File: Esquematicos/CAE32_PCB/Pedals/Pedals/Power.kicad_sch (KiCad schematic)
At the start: 16 parts, among them U5 LDL1117

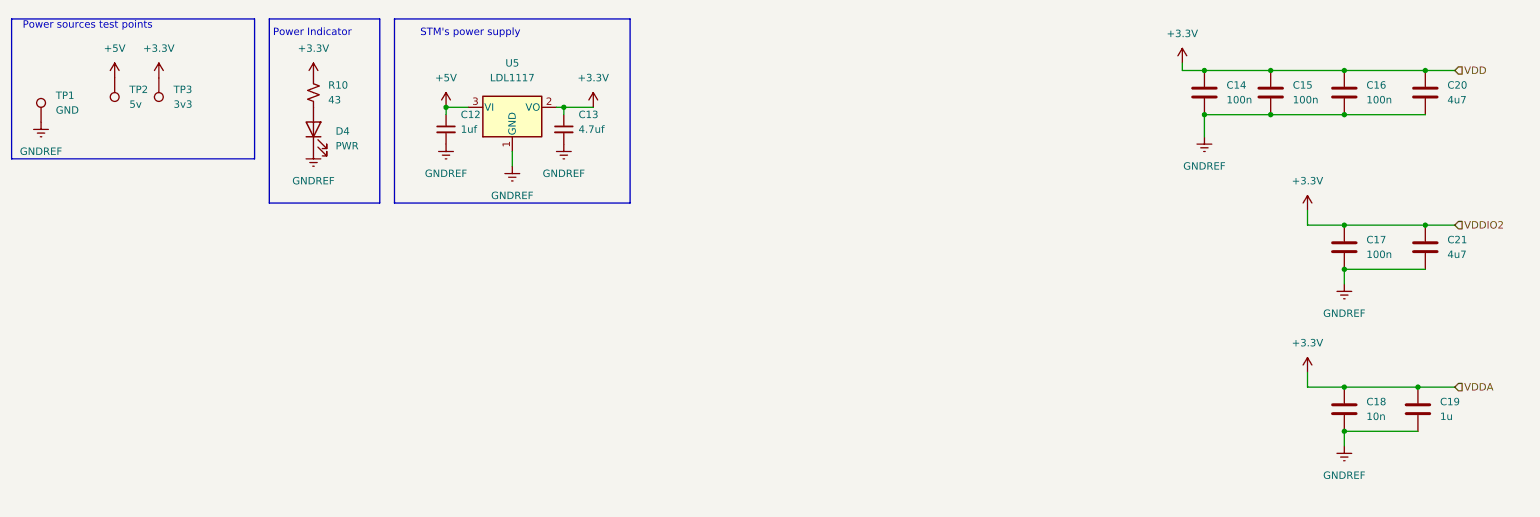
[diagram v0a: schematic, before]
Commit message: update: se añade otra hoja para las celdas de carga, ademas de reorganizar todas las hojas
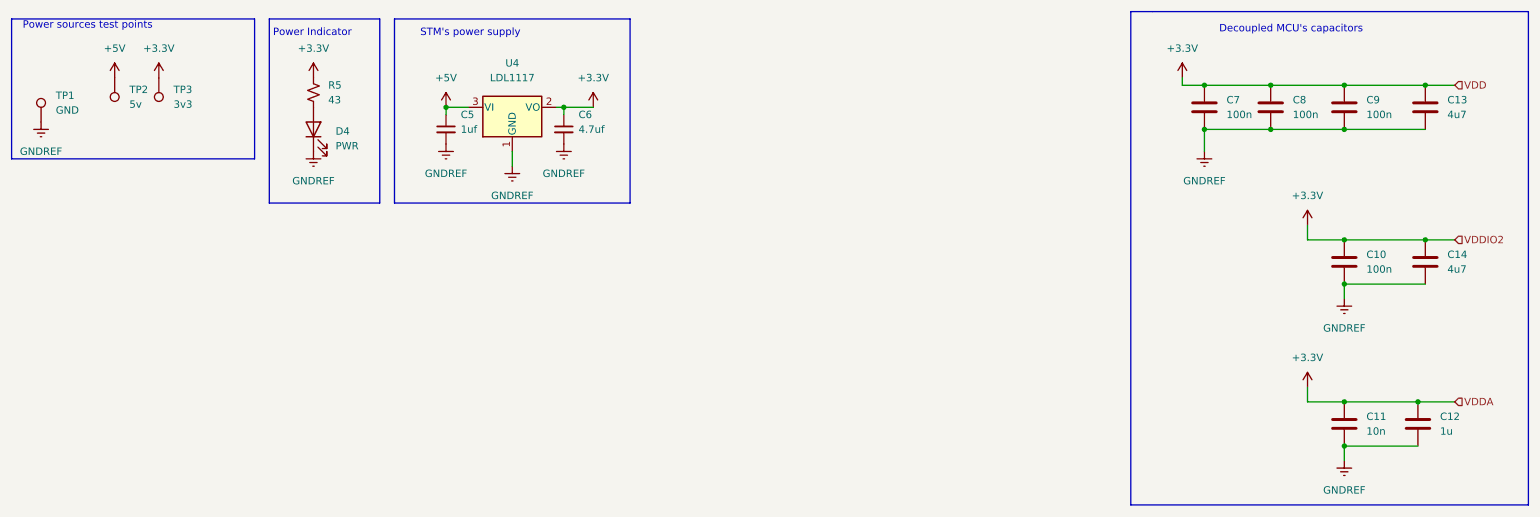
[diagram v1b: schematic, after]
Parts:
- C10: renamed from C17; footprint Capacitor_SMD:C_0805_2012Metric_Pad1.18x1.45mm_HandSolder -> Capacitor_SMD:C_0603_1608Metric_Pad1.08x0.95mm_HandSolder
- C11: renamed from C18; footprint Capacitor_SMD:C_0805_2012Metric_Pad1.18x1.45mm_HandSolder -> Capacitor_SMD:C_0603_1608Metric_Pad1.08x0.95mm_HandSolder
- C12: renamed from C19; footprint Capacitor_SMD:C_0805_2012Metric_Pad1.18x1.45mm_HandSolder -> Capacitor_SMD:C_0603_1608Metric_Pad1.08x0.95mm_HandSolder
- C13: renamed from C20; footprint Capacitor_SMD:C_0805_2012Metric_Pad1.18x1.45mm_HandSolder -> Capacitor_SMD:C_0603_1608Metric_Pad1.08x0.95mm_HandSolder
- C14: renamed from C21; footprint Capacitor_SMD:C_0805_2012Metric_Pad1.18x1.45mm_HandSolder -> Capacitor_SMD:C_0603_1608Metric_Pad1.08x0.95mm_HandSolder
- C5: renamed from C12; footprint Capacitor_SMD:C_0805_2012Metric_Pad1.18x1.45mm_HandSolder -> Capacitor_SMD:C_0603_1608Metric_Pad1.08x0.95mm_HandSolder
- C6: renamed from C13; footprint Capacitor_SMD:C_0805_2012Metric_Pad1.18x1.45mm_HandSolder -> Capacitor_SMD:C_0603_1608Metric_Pad1.08x0.95mm_HandSolder
- C7: renamed from C14; footprint Capacitor_SMD:C_0805_2012Metric_Pad1.18x1.45mm_HandSolder -> Capacitor_SMD:C_0603_1608Metric_Pad1.08x0.95mm_HandSolder
- C8: renamed from C15; footprint Capacitor_SMD:C_0805_2012Metric_Pad1.18x1.45mm_HandSolder -> Capacitor_SMD:C_0603_1608Metric_Pad1.08x0.95mm_HandSolder
- C9: renamed from C16; footprint Capacitor_SMD:C_0805_2012Metric_Pad1.18x1.45mm_HandSolder -> Capacitor_SMD:C_0603_1608Metric_Pad1.08x0.95mm_HandSolder
- renumbered R10 to R5, U5 to U4
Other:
- note added: "Decoupled MCU's capacitors"
- moved on the sheet: C10, C11, C12, C13, C14, C7, C8, C9

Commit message: update: Componentes acomodados en la PCB
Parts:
- R5: footprint Resistor_SMD:R_0805_2012Metric_Pad1.20x1.40mm_HandSolder -> Resistor_SMD:R_0603_1608Metric_Pad0.98x0.95mm_HandSolder
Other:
- moved on the sheet: C10, C11, C12, C13, C14, C7, C8, C9

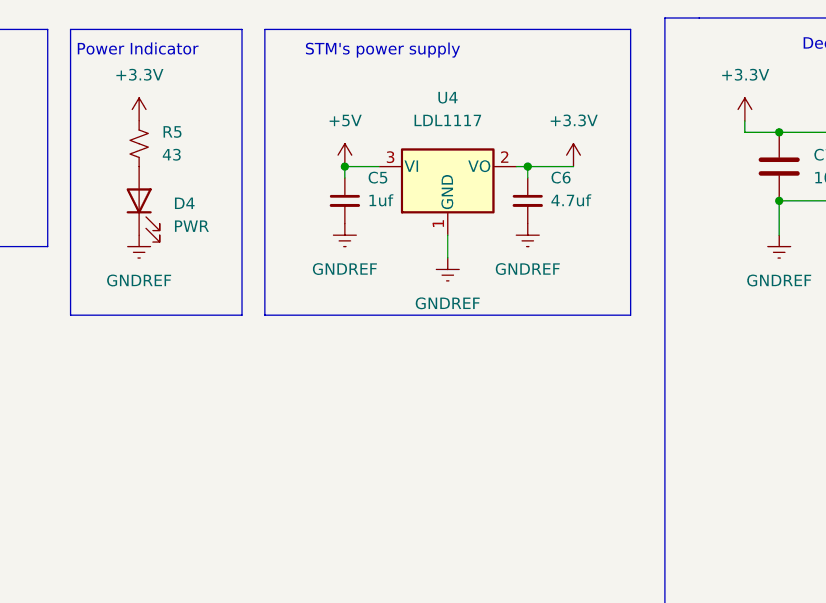
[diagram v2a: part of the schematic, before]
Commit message: update: se agrega el consumo de corriente a los IC's ademas de agregar el URL y numero de parte de los componentes de LCSC en kicad
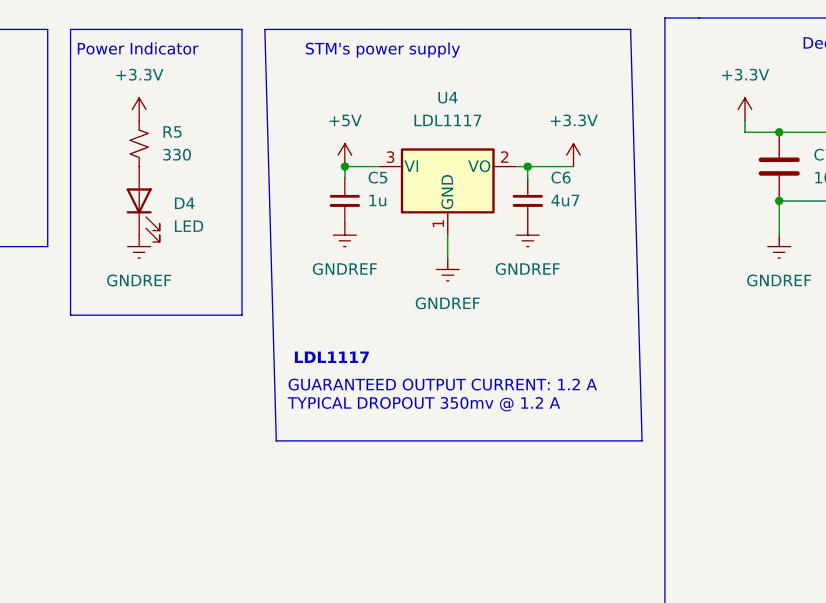
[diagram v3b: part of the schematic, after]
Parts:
- C10, C7, C8, C9: LCSC_PART (none) -> c1591
- C11: LCSC_PART (none) -> C100042
- C12: LCSC_PART (none) -> C1592
- C13, C14: LCSC_PART (none) -> C1705
- C5: value 1uf -> 1u; LCSC_PART (none) -> C1592
- C6: value 4.7uf -> 4u7; LCSC_PART (none) -> C1705
- D4: value PWR -> LED; LCSC_PART (none) -> C965815
- R5: value 43 -> 330; LCSC_PART (none) -> C25804
- U4: LCSC_PART (none) -> C2798214
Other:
- note added: "GUARANTEED OUTPUT CURRENT: 1.2 A TYPICAL DROPOUT 350mv @ 1.2 A"
- note added: "LDL1117"
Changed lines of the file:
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@@
     (stroke (width 0) (type default) (color 0 0 0 0))
   )
-  (polyline (pts (xy 125.73 21.59) (xy 125.73 53.34))
+  (polyline (pts (xy 125.73 21.59) (xy 127 67.31))
     (stroke (width 0) (type default) (color 0 0 0 0))
   )
@@
     (stroke (width 0) (type default) (color 0 0 0 0))
   )
-  (polyline (pts (xy 85.09 21.59) (xy 85.09 53.34))
+  (polyline (pts (xy 85.09 21.59) (xy 86.36 67.31))
     (stroke (width 0) (type default) (color 0 0 0 0))
   )
@@
     (stroke (width 0) (type default) (color 0 0 0 0))
   )
-  (polyline (pts (xy 125.73 53.34) (xy 85.09 53.34))
+  (polyline (pts (xy 127 67.31) (xy 86.36 67.31))
     (stroke (width 0) (type default) (color 0 0 0 0))
   )
@@
     (effects (font (size 1.27 1.27)) (justify left bottom))
   )
+  (text "GUARANTEED OUTPUT CURRENT: 1.2 A\nTYPICAL DROPOUT 350mv @ 1.2 A"
+    (at 87.63 64.135 0)
+    (effects (font (size 1.27 1.27)) (justify left bottom))
+  )
   (text "STM's power supply" (at 89.535 24.765 0)
     (effects (font (size 1.27 1.27)) (justify left bottom))
@@
   (text "Power sources test points" (at 20.955 23.495 0)
     (effects (font (size 1.27 1.27)) (justify left bottom))
+  )
+  (text "LDL1117" (at 88.265 59.055 0)
+    (effects (font (size 1.27 1.27) bold) (justify left bottom))
   )
   (hierarchical_label "VDDA" (shape input) (at 185.42 87.63 0)
@@
       (effects (font (size 1.27 1.27)) hide)
     )
+    (property "LCSC_PART" "C2798214" (id 4) (at 105.41 36.83 0)
+      (effects (font (size 1.27 1.27)) hide)
+    )
     (pin "1")
     (pin "2")
@@
     )
     (property "Datasheet" "~" (id 3) (at 166.37 36.83 0)
+      (effects (font (size 1.27 1.27)) hide)
+    )
+    (property "LCSC_PART" "c1591" (id 4) (at 166.37 36.83 0)
       (effects (font (size 1.27 1.27)) hide)
     )
@@
       (effects (font (size 1.27 1.27)) (justify left))
     )
-    (property "Value" "43" (id 1) (at 73.66 35.5599 0)
+    (property "Value" "330" (id 1) (at 73.66 35.5599 0)
       (effects (font (size 1.27 1.27)) (justify left))
     )
@@
       (effects (font (size 1.27 1.27)) hide)
     )
+    (property "LCSC_PART" "C25804" (id 4) (at 71.12 34.29 0)
+      (effects (font (size 1.27 1.27)) hide)
+    )
     (pin "1")
     (pin "2")
@@
       (effects (font (size 1.27 1.27)) hide)
     )
-    (property "Datasheet" "~" (id 3) (at 29.21 39.37 0)
+    (property "Datasheet" "" (id 3) (at 29.21 39.37 0)
+      (effects (font (size 1.27 1.27)) hide)
+    )
+    (property "LCSC_PART" "" (id 4) (at 24.13 39.37 0)
       (effects (font (size 1.27 1.27)) hide)
     )
@@
       (effects (font (size 1.27 1.27)) hide)
     )
+    (property "LCSC_PART" "C1705" (id 4) (at 180.34 63.5 0)
+      (effects (font (size 1.27 1.27)) hide)
+    )
     (pin "1")
     (pin "2")
@@
       (effects (font (size 1.27 1.27)) hide)
     )
+    (property "LCSC_PART" "c1591" (id 4) (at 166.37 63.5 0)
+      (effects (font (size 1.27 1.27)) hide)
+    )
     (pin "1")
     (pin "2")
@@
     )
     (property "Datasheet" "~" (id 3) (at 180.34 36.83 0)
+      (effects (font (size 1.27 1.27)) hide)
+    )
+    (property "LCSC_PART" "C1705" (id 4) (at 180.34 36.83 0)
       (effects (font (size 1.27 1.27)) hide)
     )
@@
       (effects (font (size 1.27 1.27)) (justify left))
     )
-    (property "Value" "4.7uf" (id 1) (at 116.84 40.64 0)
+    (property "Value" "4u7" (id 1) (at 116.84 40.64 0)
       (effects (font (size 1.27 1.27)) (justify left))
     )
@@
     )
     (property "Datasheet" "~" (id 3) (at 114.3 40.64 0)
+      (effects (font (size 1.27 1.27)) hide)
+    )
+    (property "LCSC_PART" "C1705" (id 4) (at 114.3 40.64 0)
       (effects (font (size 1.27 1.27)) hide)
     )
@@
       (effects (font (size 1.27 1.27)) hide)
     )
-    (property "Datasheet" "~" (id 3) (at 179.07 91.44 0)
+    (property "Datasheet" "" (id 3) (at 179.07 91.44 0)
+      (effects (font (size 1.27 1.27)) hide)
+    )
+    (property "LCSC_PART" "C1592" (id 4) (at 179.07 91.44 0)
       (effects (font (size 1.27 1.27)) hide)
     )
@@
     )
     (property "Datasheet" "~" (id 3) (at 142.24 36.83 0)
+      (effects (font (size 1.27 1.27)) hide)
+    )
+    (property "LCSC_PART" "c1591" (id 4) (at 142.24 36.83 0)
       (effects (font (size 1.27 1.27)) hide)
     )
@@
       (effects (font (size 1.27 1.27)) (justify left))
     )
-    (property "Value" "1uf" (id 1) (at 96.52 40.64 0)
+    (property "Value" "1u" (id 1) (at 96.52 40.64 0)
       (effects (font (size 1.27 1.27)) (justify left))
     )
@@
       (effects (font (size 1.27 1.27)) hide)
     )
-    (property "Datasheet" "~" (id 3) (at 93.98 40.64 0)
+    (property "Datasheet" "" (id 3) (at 93.98 40.64 0)
+      (effects (font (size 1.27 1.27)) hide)
+    )
+    (property "LCSC_PART" "C1592" (id 4) (at 93.98 40.64 0)
       (effects (font (size 1.27 1.27)) hide)
     )
@@
       (effects (font (size 1.27 1.27)) hide)
     )
+    (property "LCSC_PART" "C100042" (id 4) (at 166.37 91.44 0)
+      (effects (font (size 1.27 1.27)) hide)
+    )
     (pin "1")
     (pin "2")
@@
       (effects (font (size 1.27 1.27)) (justify right))
     )
-    (property "Value" "PWR" (id 1) (at 74.93 43.4974 90)
+    (property "Value" "LED" (id 1) (at 74.93 43.4974 90)
       (effects (font (size 1.27 1.27)) (justify right))
     )
@@
       (effects (font (size 1.27 1.27)) hide)
     )
-    (property "Datasheet" "~" (id 3) (at 71.12 40.64 0)
+    (property "Datasheet" "https://datasheet.lcsc.com/lcsc/2211030000_XINGLIGHT-XL-2012UGC_C965815.pdf" (id 3) (at 71.12 40.64 0)
+      (effects (font (size 1.27 1.27)) hide)
+    )
+    (property "LCSC_PART" "C965815" (id 4) (at 71.12 40.64 0)
       (effects (font (size 1.27 1.27)) hide)
     )
@@
       (effects (font (size 1.27 1.27)) hide)
     )
+    (property "LCSC_PART" "c1591" (id 4) (at 153.67 36.83 0)
+      (effects (font (size 1.27 1.27)) hide)
+    )

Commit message: Update: esquematicos de PCB, reorganizando elementos para hacer mas compacta la pcb, ademas de agregar serigrafia e imagenes de la PCB
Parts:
- TP1, TP2, TP3: footprint TestPoint:TestPoint_Pad_D3.0mm -> TestPoint:TestPoint_Pad_D1.0mm
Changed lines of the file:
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@@
       (effects (font (size 1.27 1.27)) (justify right))
     )
-    (property "Footprint" "TestPoint:TestPoint_Pad_D3.0mm" (id 2) (at 39.37 31.75 0)
+    (property "Footprint" "TestPoint:TestPoint_Pad_D1.0mm" (id 2) (at 39.37 31.75 0)
       (effects (font (size 1.27 1.27)) hide)
     )
@@
       (effects (font (size 1.27 1.27)) (justify right))
     )
-    (property "Footprint" "TestPoint:TestPoint_Pad_D3.0mm" (id 2) (at 31.75 31.75 0)
+    (property "Footprint" "TestPoint:TestPoint_Pad_D1.0mm" (id 2) (at 31.75 31.75 0)
       (effects (font (size 1.27 1.27)) hide)
     )
@@
       (effects (font (size 1.27 1.27)) (justify left))
     )
-    (property "Footprint" "TestPoint:TestPoint_Pad_D3.0mm" (id 2) (at 29.21 39.37 0)
+    (property "Footprint" "TestPoint:TestPoint_Pad_D1.0mm" (id 2) (at 29.21 39.37 0)
       (effects (font (size 1.27 1.27)) hide)
     )

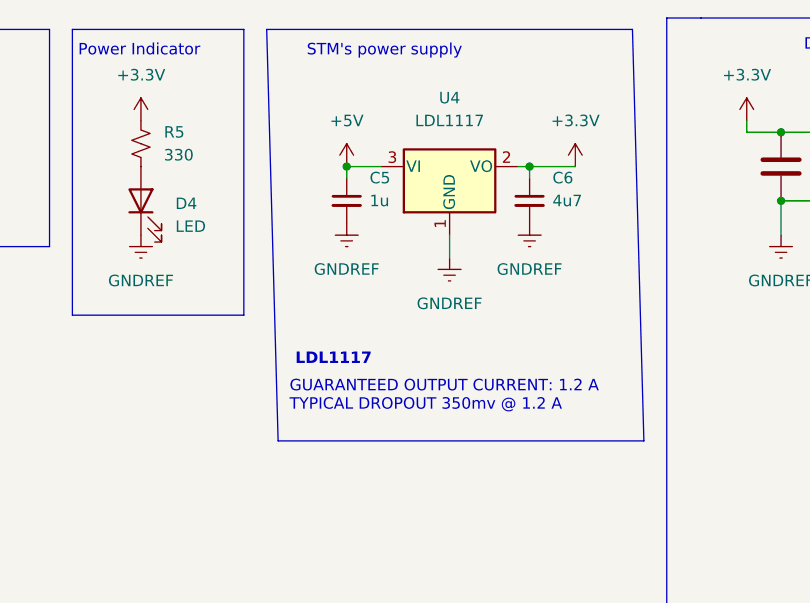
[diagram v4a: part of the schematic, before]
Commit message: update: se crea la primera revisión de la PCB
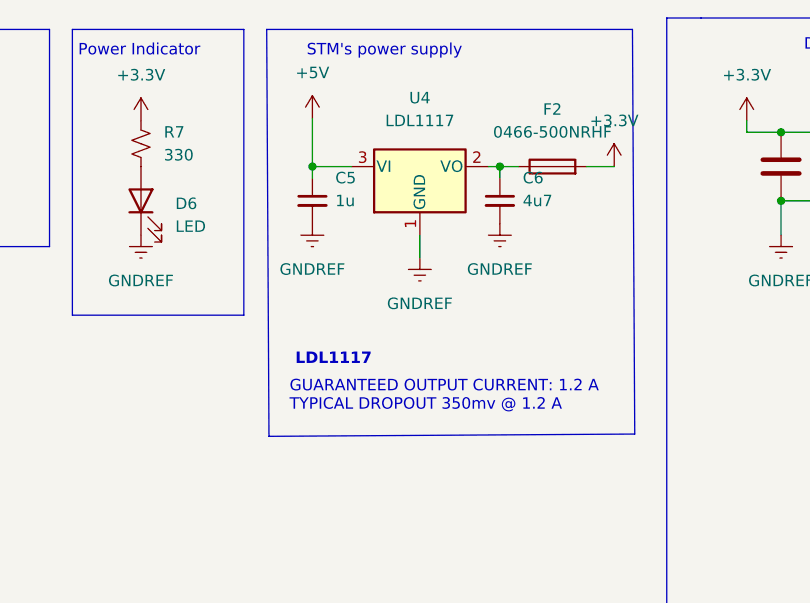
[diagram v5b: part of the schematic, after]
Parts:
- added F2: 0466-500NRHF, Fuse:Fuse_0603_1608Metric_Pad1.05x0.95mm_HandSolder, symbol Device:Fuse
- C10, C7, C8, C9: Item (none) -> c1591; Qty (none) -> 22; Vendor (none) -> c1591
- C11: Item (none) -> C100042; Qty (none) -> 1; Vendor (none) -> C100042
- C12, C5: Item (none) -> C1592; Qty (none) -> 2; Vendor (none) -> C1592
- C13, C14, C6: Item (none) -> C1705; Qty (none) -> 3; Vendor (none) -> C1705
- D6: renamed from D4; Item (none) -> C965815; Qty (none) -> 4; Vendor (none) -> C965815
- R7: renamed from R5; Item (none) -> C25804; Qty (none) -> 4; Vendor (none) -> C25804
- TP1, TP2, TP3: Qty (none) -> 1
- U4: Item (none) -> C2798214; Qty (none) -> 1; Vendor (none) -> C2798214
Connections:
- net +3.3V: now also F2.2; no longer C6.1, U4.2 (VO)
- new net: C6.1, F2.1, U4.2 (VO)
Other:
- moved on the sheet: C5, C6, U4

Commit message: chore: arrange schematics components
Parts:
- C10, C11, C12, C13, C14, C5, C6, C7, C8, C9: footprint Capacitor_SMD:C_0603_1608Metric_Pad1.08x0.95mm_HandSolder -> Capacitor_SMD:C_0603_1608Metric
- D6: footprint LED_SMD:LED_0805_2012Metric_Pad1.15x1.40mm_HandSolder -> LED_SMD:LED_0805_2012Metric
- F2: footprint Fuse:Fuse_0603_1608Metric_Pad1.05x0.95mm_HandSolder -> Fuse:Fuse_0603_1608Metric
- R7: footprint Resistor_SMD:R_0603_1608Metric_Pad0.98x0.95mm_HandSolder -> Resistor_SMD:R_0603_1608Metric
